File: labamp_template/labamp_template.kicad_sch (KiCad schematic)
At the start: 13 parts, among them J1 Conn_02x06_Odd_Even, J2 Conn_02x06_Odd_Even, J3 Conn_01x03

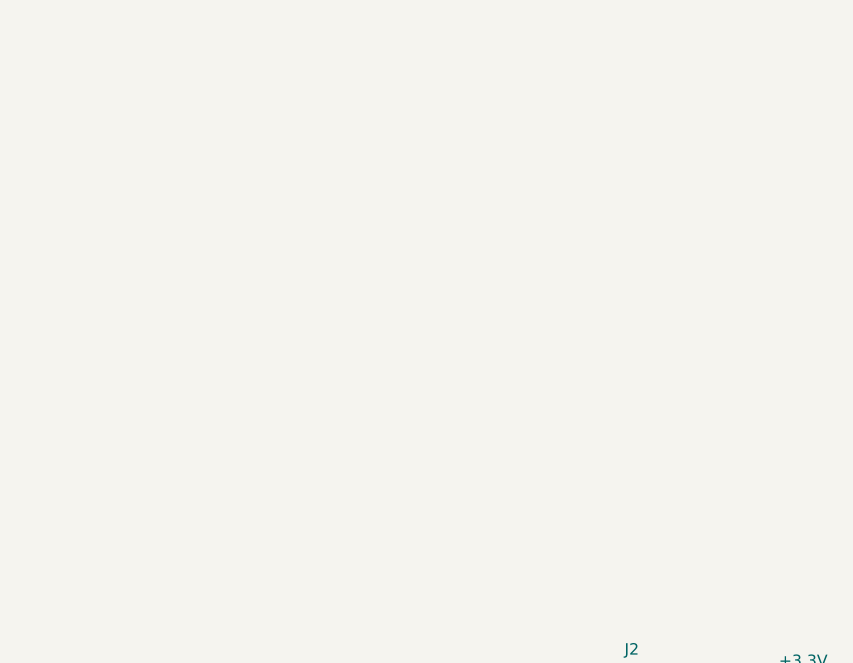
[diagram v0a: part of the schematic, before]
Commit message: Added title and subtitle to schematics template
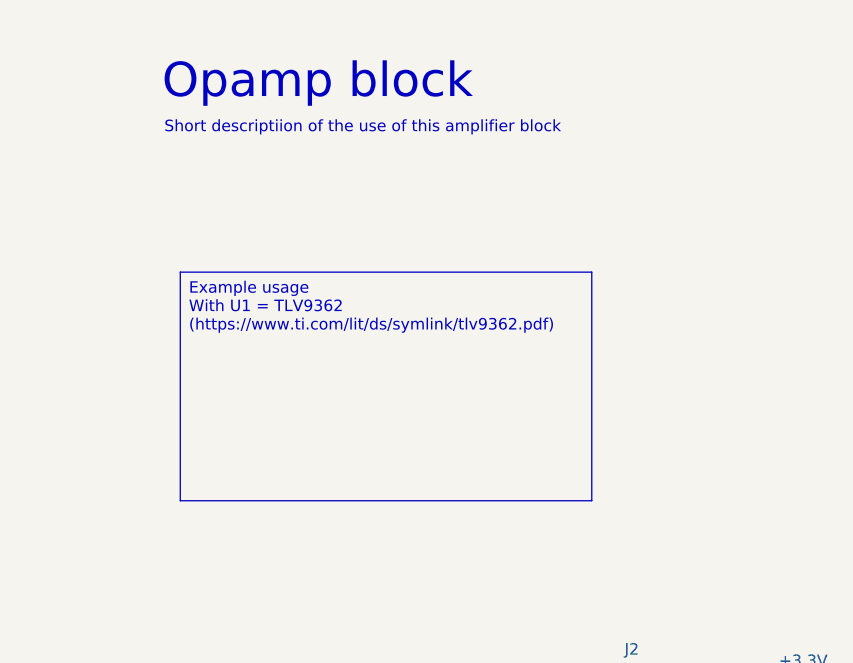
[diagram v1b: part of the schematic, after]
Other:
- note added: "Opamp block"
- note added: "Short descriptiion of the use of this amplifier block"
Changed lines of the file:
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@@
 	(generator_version "9.0")
 	(paper "A4")
+	(text "Opamp block\n"
+		(exclude_from_sim no)
+		(at 198.628 19.558 0)
+		(effects
+			(font
+				(size 3.81 3.81)
+			)
+			(justify left)
+		)
+	)
+	(text "Short descriptiion of the use of this amplifier block\n"
+		(exclude_from_sim no)
+		(at 198.882 24.638 0)
+		(effects
+			(font
+				(size 1.27 1.27)
+			)
+			(justify left)
+		)
+	)
+	(text_box "Example usage\nWith U1 = TLV9362 (https://www.ti.com/lit/ds/symlink/tlv9362.pdf)"
+		(exclude_from_sim no)
+		(at 200.66 40.64 0)
+		(size 45.72 25.4)
+		(margins 0.9525 0.9525 0.9525 0.9525)
+		(stroke
+			(width 0)
+			(type solid)
+		)
+		(fill
+			(type none)
+		)
+		(effects
+			(font
+				(size 1.27 1.27)
+			)
+			(justify left top)
+		)
+	)
 	(junction
 		(at 54.61 96.52)
